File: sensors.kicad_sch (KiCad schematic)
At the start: 21 parts, among them J501 BMV080, U501 SCD40-D-R2, U502 AS3935-BQFT, U503 BME688, U504 BME688

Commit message: Update schematic wiring
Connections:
- net AS_ANT_P: no longer C505.1, L501.1, R501.1
- new net: C505.1, L501.1, R501.1

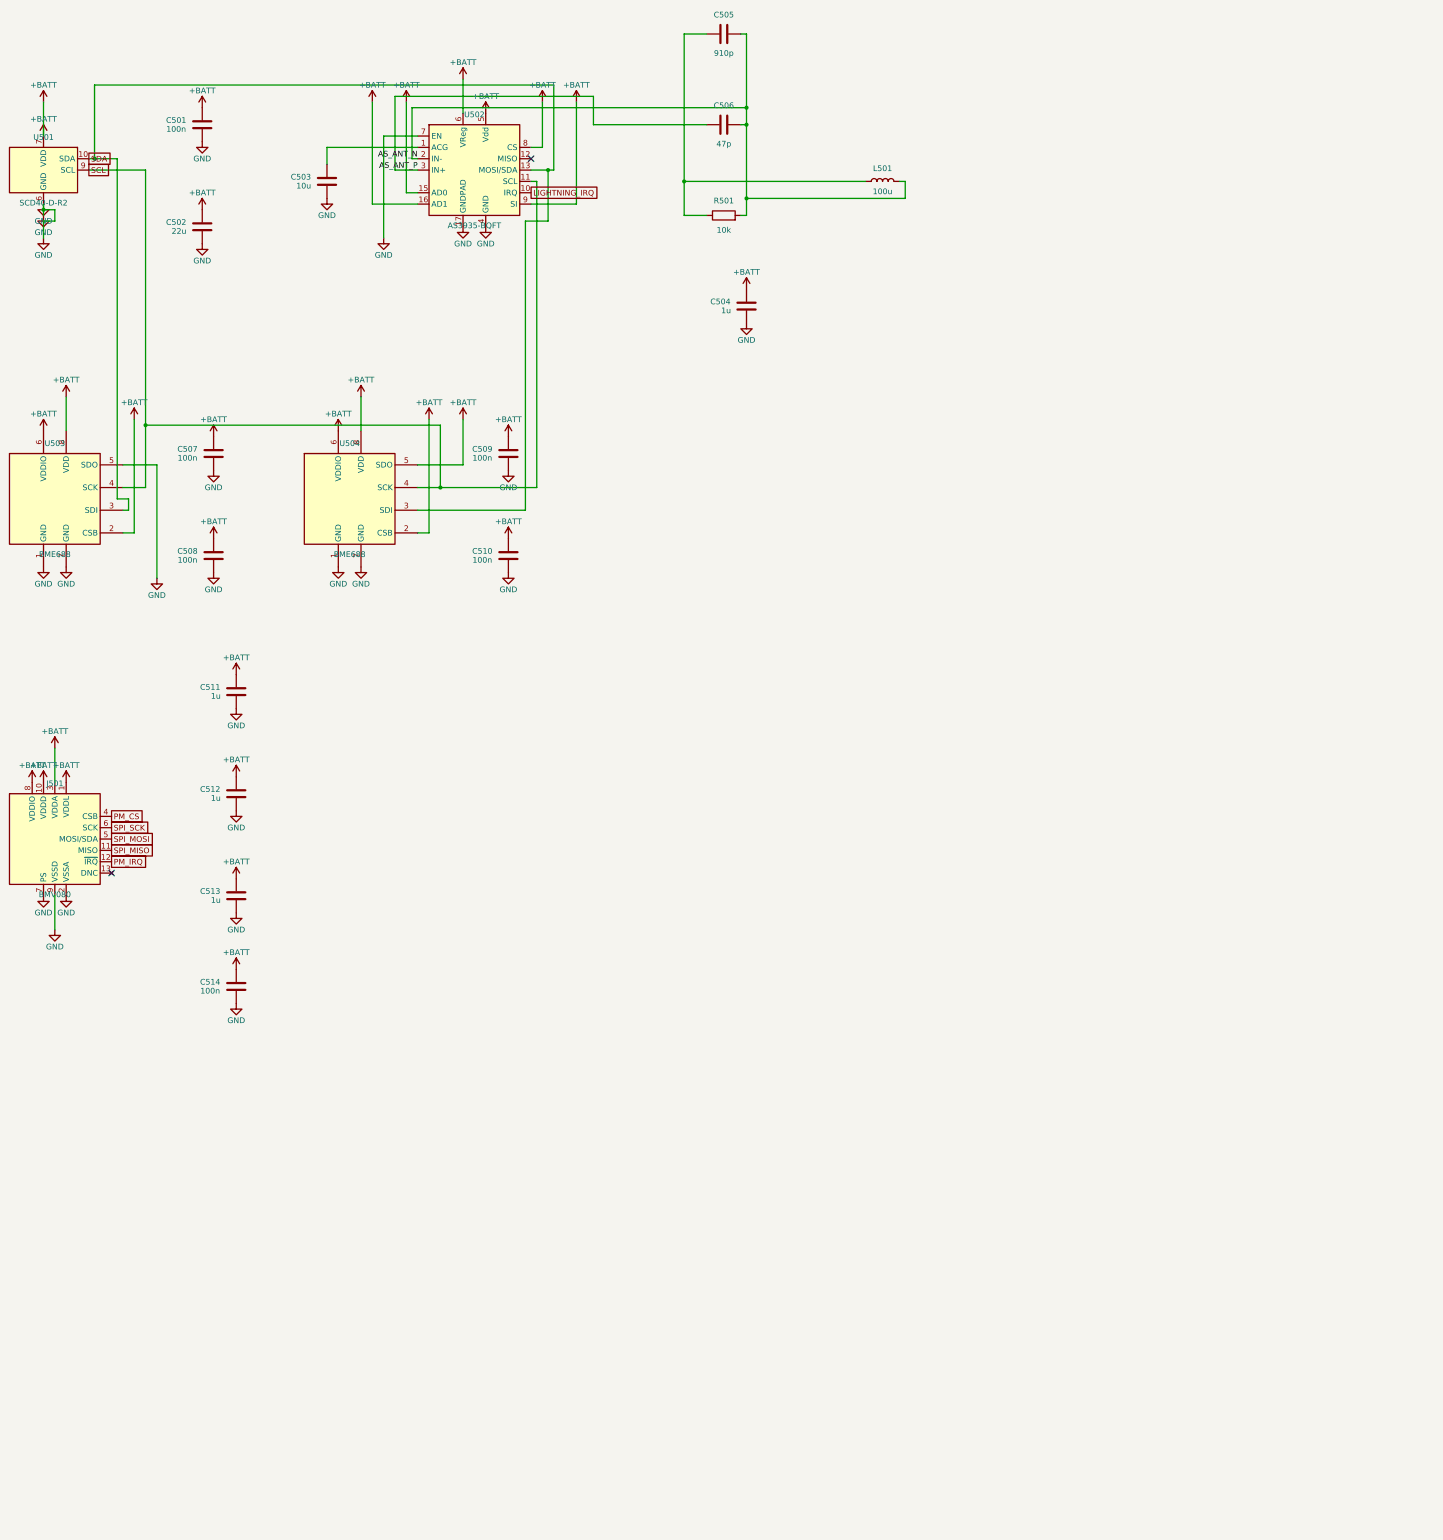
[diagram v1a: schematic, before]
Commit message: Clean up schematic. Add component groups to PCB.
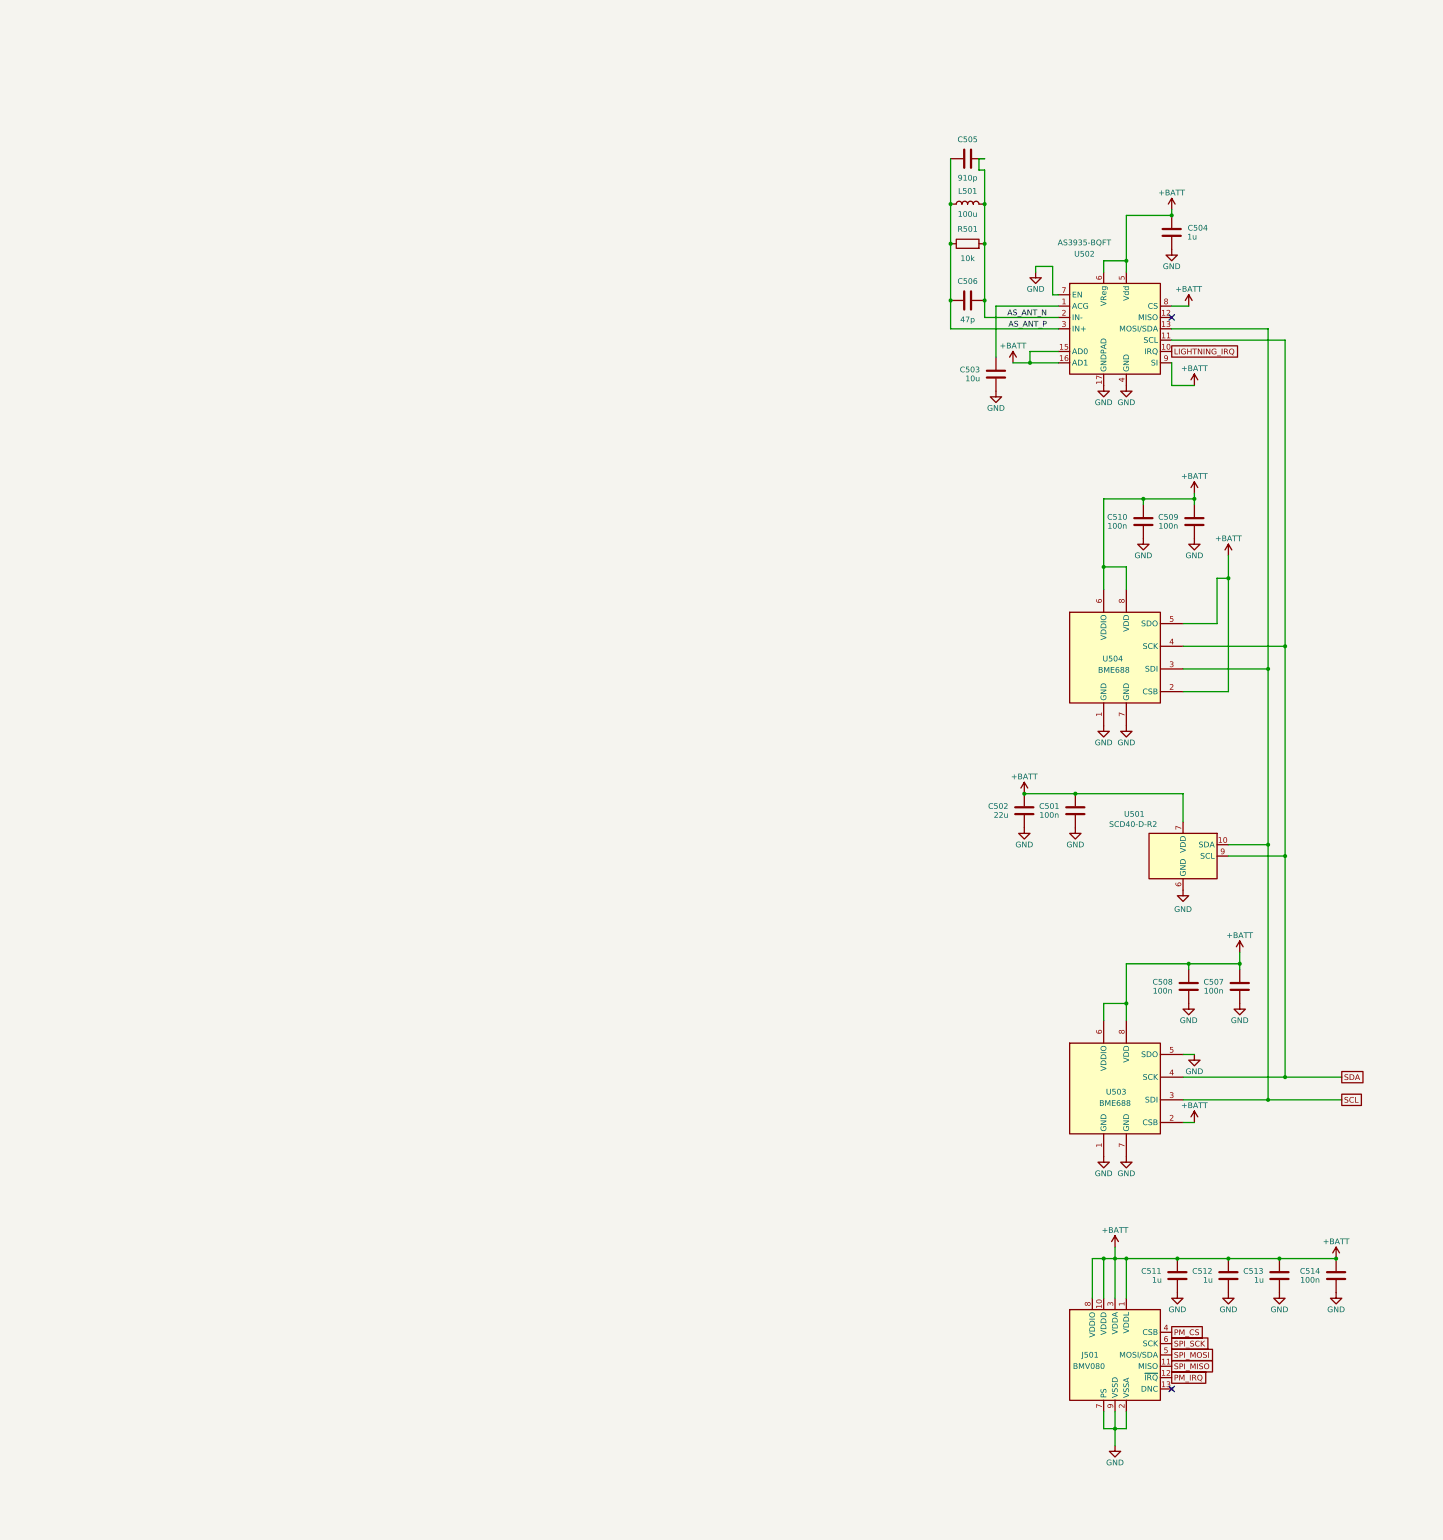
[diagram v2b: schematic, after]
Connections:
- net AS_ANT_P: now also C505.1, L501.1, R501.1
- net SCL: now also U501.10 (SDA), U502.13 (MOSI/SDA), U503.3 (SDI), U504.3 (SDI); no longer U501.9 (SCL), U502.11 (SCL), U503.4 (SCK), U504.4 (SCK)
- net SDA: now also U501.9 (SCL), U502.11 (SCL), U503.4 (SCK), U504.4 (SCK); no longer U501.10 (SDA), U502.13 (MOSI/SDA), U503.3 (SDI), U504.3 (SDI)
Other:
- moved on the sheet: C501, C502, C503, C504, C505, C506, C507, C508, C509, C510, C511, C512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

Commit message: Inital routing
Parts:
- removed C502: 22u, Capacitor_SMD:C_0805_2012Metric, symbol Device:C
- removed C512, C513: 1u, Capacitor_SMD:C_0402_1005Metric, symbol Device:C
- removed C514: 100n, Capacitor_SMD:C_0402_1005Metric, symbol Device:C
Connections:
- net SCL: now also U501.9 (SCL), U502.11 (SCL), U503.4 (SCK), U504.4 (SCK); no longer U501.10 (SDA), U502.13 (MOSI/SDA), U503.3 (SDI), U504.3 (SDI)
- net SDA: now also U501.10 (SDA), U502.13 (MOSI/SDA), U503.3 (SDI), U504.3 (SDI); no longer U501.9 (SCL), U502.11 (SCL), U503.4 (SCK), U504.4 (SCK)
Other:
- moved on the sheet: C507, C508

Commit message: Route, mostly done.
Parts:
- added JP1: IAB0, cc1200_balloon:Jumper_3_0402, symbol Jumper:SolderJumper_3_Open
- added JP2: IAB1, cc1200_balloon:Jumper_3_0402, symbol Jumper:SolderJumper_3_Open
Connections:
- net SPI_MOSI is gone; now on net SDA: J501.5 (MOSI/SDA)
- net SPI_SCK is gone; now on net SCL: J501.6 (SCK)
- net +BATT: now also J501.7 (PS), JP1.3 (B), JP2.3 (B)
- net GND: now also JP1.1 (A), JP2.1 (A); no longer J501.7 (PS)
- net PM_CS renamed IAB0
- net IAB0: now also JP1.2 (C)
- net SPI_MISO renamed IAB1
- net IAB1: now also JP2.2 (C)
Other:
- moved on the sheet: C511, J501

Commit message: Fix DRC errors.
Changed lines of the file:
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@@
-	)
-	(junction
-		(at 303.53 157.48)
-		(diameter 0)
-		(color 0 0 0 0)
 	)
 	(junction
@@
 	(junction
 		(at 248.92 95.25)
+		(diameter 0)
+		(color 0 0 0 0)
+	)
+	(junction
+		(at 303.53 167.64)
 		(diameter 0)
 		(color 0 0 0 0)
@@
 	(wire
 		(pts
-			(xy 300.99 157.48) (xy 303.53 157.48)
-		)
-		(stroke
-			(width 0)
-			(type default)
-		)
-	)
-	(wire
-		(pts
 			(xy 279.4 349.25) (xy 279.4 347.98)
 		)
@@
 	(wire
 		(pts
+			(xy 303.53 167.64) (xy 303.53 182.88)
+		)
+		(stroke
+			(width 0)
+			(type default)
+		)
+	)
+	(wire
+		(pts
 			(xy 275.59 139.7) (xy 284.48 139.7)
 		)
@@
 	(wire
 		(pts
-			(xy 293.37 167.64) (xy 300.99 167.64)
+			(xy 293.37 167.64) (xy 303.53 167.64)
 		)
 		(stroke
@@
 	(wire
 		(pts
-			(xy 303.53 152.4) (xy 303.53 157.48)
+			(xy 303.53 152.4) (xy 303.53 167.64)
 		)
 		(stroke
@@
 	(wire
 		(pts
-			(xy 300.99 157.48) (xy 300.99 167.64)
-		)
-		(stroke
-			(width 0)
-			(type default)
-		)
-	)
-	(wire
-		(pts
 			(xy 316.23 328.93) (xy 316.23 269.24)
 		)
@@
 		)
 		(stroke
-			(width 0)
-			(type default)
-		)
-	)
-	(wire
-		(pts
-			(xy 303.53 157.48) (xy 303.53 182.88)
-		)
-		(stroke
